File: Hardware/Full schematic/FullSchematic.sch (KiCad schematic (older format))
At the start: 28 parts, among them J1 Conn_01x02, J2 Conn_01x02, J3 Conn_01x02, J4 Conn_01x02, U1 LM358

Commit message: Created VCO testing board
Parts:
- J1, J2, J3, J4: symbol Conn_01x02 -> CONN_01X02
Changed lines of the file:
@@
 EESchema Schematic File Version 2
+LIBS:FullSchematic-rescue
 LIBS:power
 LIBS:device
-LIBS:switches
-LIBS:relays
-LIBS:motors
 LIBS:transistors
 LIBS:conn
@@
 LIBS:valves
 LIBS:fossa library
-LIBS:VCO-cache
+LIBS:FullSchematic-cache
 EELAYER 25 0
 EELAYER END
@@
 encoding utf-8
 Sheet 1 1
-Title "VCO (GPLv3+)"
+Title "Full device (GPLv3+)"
 Date "2018-08-12"
 Rev "2"
@@
 $EndComp
 $Comp
-L Conn_01x02 J1
+L CONN_01X02 J1
 U 1 1 5B720BFC
-P 3550 1900
-F 0 "J1" H 3550 2000 50  0000 C CNN
-F 1 "Conn_01x02" H 3550 1700 50  0000 C CNN
-F 2 "" H 3550 1900 50  0001 C CNN
-F 3 "" H 3550 1900 50  0001 C CNN
-	1    3550 1900
+P 3550 1950
+F 0 "J1" H 3550 2050 50  0000 C CNN
+F 1 "Conn_01x02" H 3550 1750 50  0000 C CNN
+F 2 "" H 3550 1950 50  0001 C CNN
+F 3 "" H 3550 1950 50  0001 C CNN
+	1    3550 1950
 	-1   0    0    -1
 $EndComp
@@
 Tune
 $Comp
-L Conn_01x02 J2
+L CONN_01X02 J2
 U 1 1 5B7237EE
 P 8600 1050
@@
 $EndComp
 $Comp
-L Conn_01x02 J4
+L CONN_01X02 J4
 U 1 1 5B726E8F
-P 9600 2325
-F 0 "J4" H 9600 2425 50  0000 C CNN
-F 1 "Conn_01x02" H 9600 2125 50  0000 C CNN
-F 2 "" H 9600 2325 50  0001 C CNN
-F 3 "" H 9600 2325 50  0001 C CNN
-	1    9600 2325
+P 9600 2375
+F 0 "J4" H 9600 2475 50  0000 C CNN
+F 1 "Conn_01x02" H 9600 2175 50  0000 C CNN
+F 2 "" H 9600 2375 50  0001 C CNN
+F 3 "" H 9600 2375 50  0001 C CNN
+	1    9600 2375
 	1    0    0    -1
 $EndComp
@@
 	1    0    0    -1
 $EndComp
-Text Notes 9700 2400 0    60   ~ 0
+Text Notes 9700 2450 0    60   ~ 0
 Out
 $Comp
@@
 Connection ~ 8400 3475
 $Comp
-L Conn_01x02 J3
+L CONN_01X02 J3
 U 1 1 5BA77BC4
-P 8700 3475
-F 0 "J3" H 8700 3575 50  0000 C CNN
-F 1 "Conn_01x02" H 8700 3275 50  0000 C CNN
-F 2 "" H 8700 3475 50  0001 C CNN
-F 3 "" H 8700 3475 50  0001 C CNN
-	1    8700 3475
-	1    0    0    -1
-$EndComp
-Text Notes 9875 2425 0    60   ~ 0
+P 8700 3525
+F 0 "J3" H 8700 3625 50  0000 C CNN
+F 1 "Conn_01x02" H 8700 3325 50  0000 C CNN
+F 2 "" H 8700 3525 50  0001 C CNN
+F 3 "" H 8700 3525 50  0001 C CNN
+	1    8700 3525
+	1    0    0    -1
+$EndComp
+Text Notes 9875 2475 0    60   ~ 0
 1V peak to peak\n3.5MHz
 Text Notes 8800 3550 0    60   ~ 0

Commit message: Tuning to avoid 6V source instability and make startup stable
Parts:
- removed C6: 0.1uF, symbol C
- C3: value 47pF -> 100pF
- L1: value 27 uH -> 22 uH
- R8: value 110k -> 36k
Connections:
- wire segments 69 -> 68
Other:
- note added: "0V - \nxV - 3.5 MHz\nxV - 3.575 MHz\nxV - 3.65 MHz\n12V -"
- note added: "1.5V peak to peak\n3.5MHz"
- note added: "Signal ground - 6V\nAvoid capacitive load,\nparasitic oscillations may appear!"
- note removed: "1V peak to peak\n3.5MHz"
- note removed: "Signal ground - 6V"
- moved on the sheet: J2
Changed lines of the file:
@@
 P 6500 1550
 F 0 "C3" H 6525 1650 50  0000 L CNN
-F 1 "47pF" H 6525 1450 50  0000 L CNN
+F 1 "100pF" H 6525 1450 50  0000 L CNN
 F 2 "" H 6538 1400 50  0001 C CNN
 F 3 "" H 6500 1550 50  0001 C CNN
@@
 L CONN_01X02 J2
 U 1 1 5B7237EE
-P 8600 1050
-F 0 "J2" H 8600 1150 50  0000 C CNN
-F 1 "Conn_01x02" H 8600 850 50  0000 C CNN
-F 2 "" H 8600 1050 50  0001 C CNN
-F 3 "" H 8600 1050 50  0001 C CNN
-	1    8600 1050
+P 8600 1100
+F 0 "J2" H 8600 1200 50  0000 C CNN
+F 1 "Conn_01x02" H 8600 900 50  0000 C CNN
+F 2 "" H 8600 1100 50  0001 C CNN
+F 3 "" H 8600 1100 50  0001 C CNN
+	1    8600 1100
 	1    0    0    -1
 $EndComp
@@
 P 5600 1975
 F 0 "L1" V 5550 1975 50  0000 C CNN
-F 1 "27 uH" V 5710 1975 50  0000 C CNN
+F 1 "22 uH" V 5710 1975 50  0000 C CNN
 F 2 "" H 5600 1975 50  0001 C CNN
 F 3 "" H 5600 1975 50  0001 C CNN
@@
 P 9050 2325
 F 0 "R8" V 9130 2325 50  0000 C CNN
-F 1 "110k" V 9050 2325 50  0000 C CNN
+F 1 "36k" V 9050 2325 50  0000 C CNN
 F 2 "" V 8980 2325 50  0001 C CNN
 F 3 "" H 9050 2325 50  0001 C CNN
@@
 Wire Wire Line
 	6325 3375 6500 3375
-Wire Wire Line
-	6425 3575 6425 3025
 $Comp
 L +12V #PWR9
@@
 	1    0    0    -1
 $EndComp
-Wire Wire Line
-	6425 3025 7150 3025
 Connection ~ 7150 3475
 $Comp
@@
 Wire Wire Line
 	7100 3475 8500 3475
-Wire Wire Line
-	7150 3025 7150 3625
-Wire Wire Line
-	7150 4000 7150 3925
-$Comp
-L C C6
-U 1 1 5B78B961
-P 7150 3775
-F 0 "C6" H 7175 3875 50  0000 L CNN
-F 1 "0.1uF" H 7175 3675 50  0000 L CNN
-F 2 "" H 7188 3625 50  0001 C CNN
-F 3 "" H 7150 3775 50  0001 C CNN
-	1    7150 3775
-	1    0    0    -1
-$EndComp
-$Comp
-L GND #PWR14
-U 1 1 5B78B9B8
-P 7150 4000
-F 0 "#PWR14" H 7150 3750 50  0001 C CNN
-F 1 "GND" H 7150 3850 50  0000 C CNN
-F 2 "" H 7150 4000 50  0001 C CNN
-F 3 "" H 7150 4000 50  0001 C CNN
-	1    7150 4000
-	1    0    0    -1
-$EndComp
 Connection ~ 4650 2000
 Wire Wire Line
@@
 $EndComp
 Text Notes 9875 2475 0    60   ~ 0
-1V peak to peak\n3.5MHz
-Text Notes 8800 3550 0    60   ~ 0
-Signal ground - 6V
+1.5V peak to peak\n3.5MHz
+Text Notes 8850 3650 0    60   ~ 0
+Signal ground - 6V\nAvoid capacitive load,\nparasitic oscillations may appear!
+Wire Wire Line
+	7150 3475 7150 3100
+Wire Wire Line
+	7150 3100 6425 3100
+Wire Wire Line
+	6425 3100 6425 3575
+Text Notes 3225 1700 0    60   ~ 0
+0V - \nxV - 3.5 MHz\nxV - 3.575 MHz\nxV - 3.65 MHz\n12V -
 $EndSCHEMATC

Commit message: Modifid oscillator (see full schematic) to use 0V-5V tuning voltage.
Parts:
- removed unit 1 of U1
- added VD1: BB135, symbol BB135
- L1: value 22 uH -> 16 uH
- R8: value 36k -> 47k
- renumbered C7 to C6, C8 to C7, VD1 to VD2, VD2 to VD3
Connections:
- wire segments 68 -> 62
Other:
- note added: "0V - 3.152 MHz\n1.45V - 3.5 MHz\n2.02V - 3.575 MHz\n2.75V - 3.65 MHz\n5V - 3.817 MHz"
- note added: "1.7V peak to peak\n3.5MHz"
- note removed: "0V - \nxV - 3.5 MHz\nxV - 3.575 MHz\nxV - 3.65 MHz\n12V -"
- note removed: "1.5V peak to peak\n3.5MHz"
- moved on the sheet: J1, R1, VD2

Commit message: Started experimental firmware implementation
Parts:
- removed C2: 0.1uF, symbol C
- removed J2, J3: Conn_01x02, symbol CONN_01X02
- removed R2, R3: 47k, symbol R
- removed U1: LM358, symbol LM358
- added C12: 0.1uF, symbol FullSchematic-rescue:C
- added C? (x3): 0.1uF, symbol Device:C
- added C?: 100pF, symbol Device:C
- added J? (x2): Conn_01x02_Female, symbol Connector:Conn_01x02_Female
- added J?: Conn_01x04_Female, symbol Connector:Conn_01x04_Female
- added R? (x2): 4.7k, symbol Device:R
- added R?: 18k, symbol Device:R
- added U?: ADF4001, symbol Fossa_library:ADF4001
- added X?: XO53, Oscillator:Oscillator_SMD_EuroQuartz_XO53-4Pin_5.0x3.2mm, symbol Oscillator:XO53
- C1: symbol C -> FullSchematic-rescue:C
- C2: renamed from C3; symbol C -> FullSchematic-rescue:C
- C3: renamed from C4; symbol C -> FullSchematic-rescue:C
- C4: renamed from C5; symbol C -> FullSchematic-rescue:C
- C5: renamed from C6; symbol C -> FullSchematic-rescue:C
- C6: renamed from C7; symbol C -> FullSchematic-rescue:C
- D1, D2: symbol D -> FullSchematic-rescue:D
- DA1: symbol AD8031 -> FullSchematic-rescue:AD8031
- J1, J4: symbol CONN_01X02 -> FullSchematic-rescue:CONN_01X02
- L1: symbol L_Core_Ferrite -> FullSchematic-rescue:L_Core_Ferrite
- R1: symbol R -> FullSchematic-rescue:R
- R2: renamed from R4; symbol R -> FullSchematic-rescue:R
- R3: renamed from R5; symbol R -> FullSchematic-rescue:R
- R4: renamed from R6; symbol R -> FullSchematic-rescue:R
- R5: renamed from R7; symbol R -> FullSchematic-rescue:R
- R6: renamed from R8; symbol R -> FullSchematic-rescue:R
- VD1, VD2, VD3: symbol BB135 -> FullSchematic-rescue:BB135
- VT1: symbol BF862 -> FullSchematic-rescue:BF862
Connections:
- net labels added: +5V, 8MHz_5V_Ref, Fvco3.5, PLL_CLK, PLL_DATA, PLL_LE
- wire segments 62 -> 111
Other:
- note added: "+12V filtered"
- note added: "+5V filtered"
- note added: "0.4V P-P"
- note added: "8 MHz"
- note removed: "+12V"
- note removed: "GND"
- note removed: "Signal ground - 6V\nAvoid capacitive load,\nparasitic oscillations may appear!"
- moved on the sheet: J4, R4, R5

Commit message: Got SPI signal for PLL, some more driver work needed
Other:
- note added: "CLK - PA5\nDATA - PA7\nLE - PA8"
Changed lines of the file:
@@
 Text Notes 4325 4150 0    50   ~ 0
 0.4V P-P
+Text Notes 5400 5100 0    50   ~ 0
+CLK - PA5\nDATA - PA7\nLE - PA8
 $EndSCHEMATC

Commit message: PLL is controllable, Fvco is too weak
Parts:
- removed J1: Conn_01x02, symbol FullSchematic-rescue:CONN_01X02
- added C11: 0.47uF, symbol Device:C
- added C13: 4.7uF, symbol Device:CP
- added R10: 20, symbol Device:R
- gave numbers to parts that had none: 12
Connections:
- net GND: now also C11.2, C13.2
- net Vtune3.5: now reaches R1.2
- net Vtune3.5: now also U1.2 (CP), C11.1, R10.1
- new net: C13.1, R10.2
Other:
- note added: "Kvco=0.133MHz/V"
- note removed: "Tune"

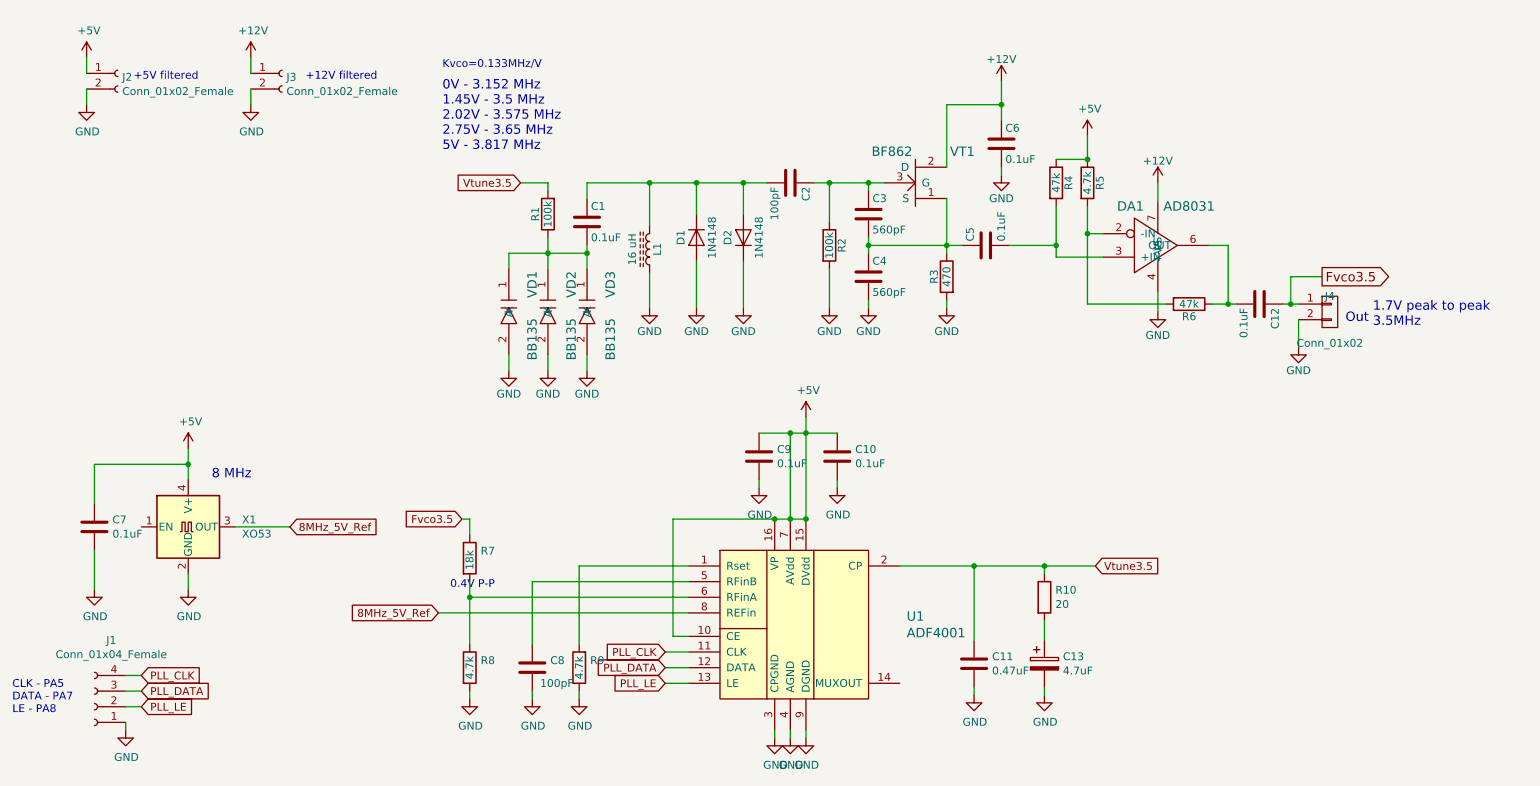
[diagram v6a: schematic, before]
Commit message: Some problems with initialization, but works in general
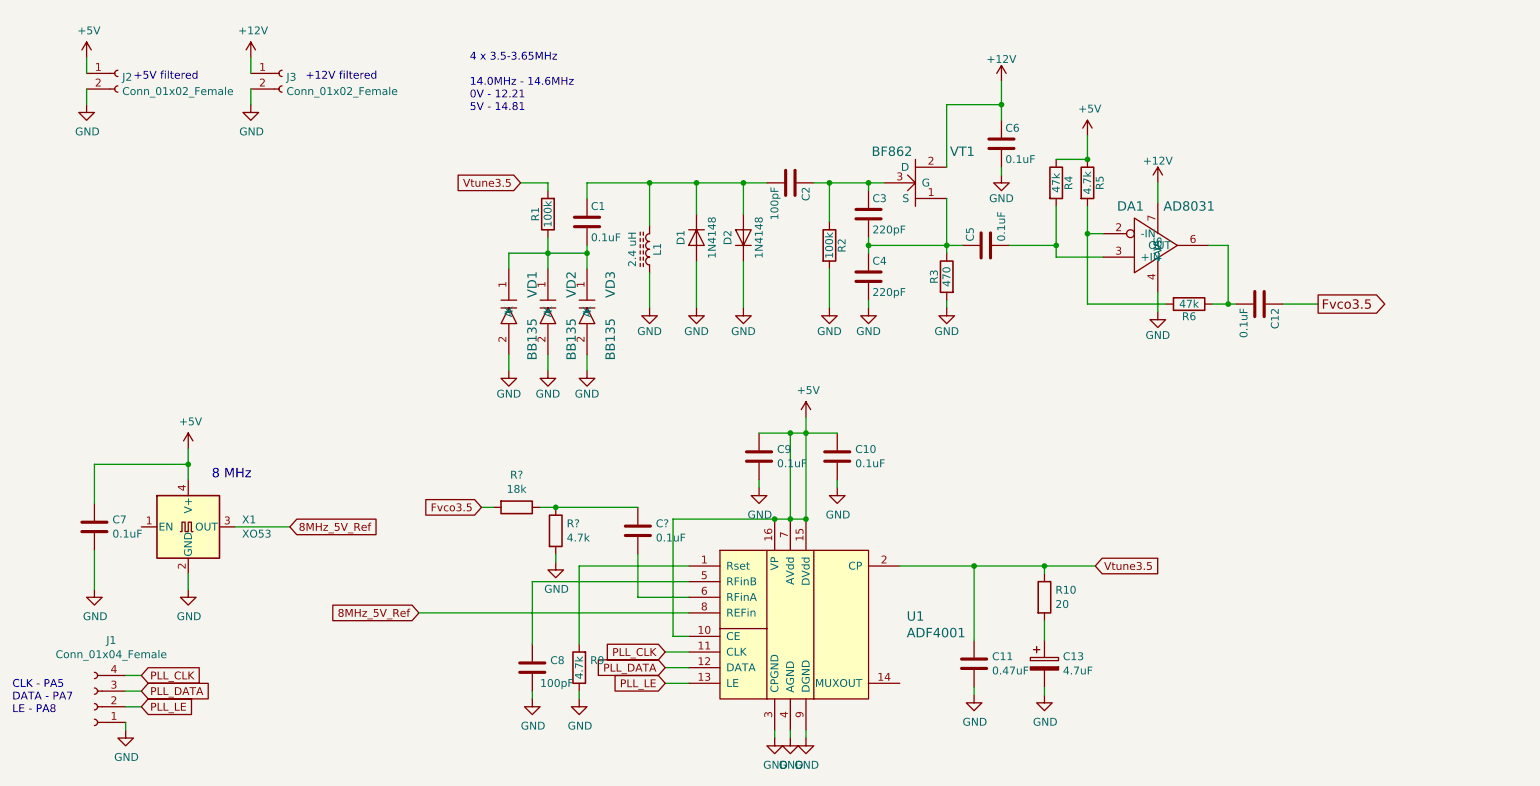
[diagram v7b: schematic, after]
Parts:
- removed J4: Conn_01x02, symbol FullSchematic-rescue:CONN_01X02
- removed R7: 18k, symbol Device:R
- removed R8: 4.7k, symbol Device:R
- added C?: 0.1uF, symbol Device:C
- added R?: 4.7k, symbol Device:R
- added R?: 18k, symbol Device:R
- C3, C4: value 560pF -> 220pF
- L1: value 16 uH -> 2.4 uH
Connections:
- net Fvco3.5: now also R?.2
- net GND: now also R?.2
- net at U1.6 (RFinA): now also C?.2
- new net: C?.1, R?.1, R?.1
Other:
- note added: "4 x 3.5-3.65MHz\n\n14.0MHz - 14.6MHz\n0V - 12.21\n5V - 14.81"
- note removed: "0.4V P-P"
- note removed: "0V - 3.152 MHz\n1.45V - 3.5 MHz\n2.02V - 3.575 MHz\n2.75V - 3.65 MHz\n5V - 3.817 MHz"
- note removed: "1.7V peak to peak\n3.5MHz"
- note removed: "Kvco=0.133MHz/V"
- note removed: "Out"
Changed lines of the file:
@@
 P 7000 1750
 F 0 "C3" H 7025 1850 50  0000 L CNN
-F 1 "560pF" H 7025 1650 50  0000 L CNN
+F 1 "220pF" H 7025 1650 50  0000 L CNN
 F 2 "" H 7038 1600 50  0001 C CNN
 F 3 "" H 7000 1750 50  0001 C CNN
@@
 P 7000 2150
 F 0 "C4" H 7025 2250 50  0000 L CNN
-F 1 "560pF" H 7025 2050 50  0000 L CNN
+F 1 "220pF" H 7025 2050 50  0000 L CNN
 F 2 "" H 7038 2000 50  0001 C CNN
 F 3 "" H 7000 2150 50  0001 C CNN
@@
 $EndComp
 $Comp
-L FullSchematic-rescue:CONN_01X02 J4
-U 1 1 5B726E8F
-P 9950 2375
-F 0 "J4" H 9950 2475 50  0000 C CNN
-F 1 "Conn_01x02" H 9950 2175 50  0000 C CNN
-F 2 "" H 9950 2375 50  0001 C CNN
-F 3 "" H 9950 2375 50  0001 C CNN
-	1    9950 2375
-	1    0    0    -1
-$EndComp
-$Comp
-L FullSchematic-rescue:GND #PWR018
-U 1 1 5B72709E
-P 9750 2600
-F 0 "#PWR018" H 9750 2350 50  0001 C CNN
-F 1 "GND" H 9750 2450 50  0000 C CNN
-F 2 "" H 9750 2600 50  0001 C CNN
-F 3 "" H 9750 2600 50  0001 C CNN
-	1    9750 2600
-	1    0    0    -1
-$EndComp
-Text Notes 10050 2450 0    60   ~ 0
-Out
-$Comp
 L FullSchematic-rescue:GND #PWR05
 U 1 1 5B7892C1
@@
 P 5600 1975
 F 0 "L1" V 5550 1975 50  0000 C CNN
-F 1 "16 uH" V 5710 1975 50  0000 C CNN
+F 1 "2.4 uH" V 5710 1975 50  0000 C CNN
 F 2 "" H 5600 1975 50  0001 C CNN
 F 3 "" H 5600 1975 50  0001 C CNN
@@
 	1    0    0    -1
 $EndComp
-Text Notes 10225 2475 0    60   ~ 0
-1.7V peak to peak\n3.5MHz
-Text Notes 4275 1350 0    60   ~ 0
-0V - 3.152 MHz\n1.45V - 3.5 MHz\n2.02V - 3.575 MHz\n2.75V - 3.65 MHz\n5V - 3.817 MHz
 $Comp
 L FullSchematic-rescue:BB135 VD1
@@
 	1    0    0    -1
 $EndComp
-Text GLabel 9900 2150 2    60   Output ~ 0
+Text GLabel 9875 2325 2    60   Output ~ 0
 Fvco3.5
 Wire Wire Line
@@
 $EndComp
 Wire Wire Line
-	9750 2325 9700 2325
-Wire Wire Line
-	9750 2425 9750 2600
-Wire Wire Line
-	9900 2150 9700 2150
-Wire Wire Line
-	9700 2150 9700 2325
-Connection ~ 9700 2325
-Wire Wire Line
 	7850 1050 7850 1150
 Wire Wire Line
@@
 Wire Wire Line
 	4950 2000 4950 2100
-Wire Wire Line
-	9700 2325 9650 2325
 $Comp
 L Oscillator:XO53 X1
@@
 Wire Wire Line
 	4850 4100 5850 4100
-Text GLabel 4250 4300 0    50   Input ~ 0
+Text GLabel 4125 4300 0    50   Input ~ 0
 8MHz_5V_Ref
-Wire Wire Line
-	5850 4300 4250 4300
-$Comp
-L Device:R R8
-U 1 1 5FE0D1B7
-P 4450 4650
-F 0 "R8" H 4520 4696 50  0000 L CNN
-F 1 "4.7k" V 4450 4575 50  0000 L CNN
-F 2 "" V 4380 4650 50  0001 C CNN
-F 3 "~" H 4450 4650 50  0001 C CNN
-	1    4450 4650
-	1    0    0    -1
-$EndComp
-$Comp
-L FullSchematic-rescue:GND #PWR023
-U 1 1 5FE0EF2A
-P 4450 4850
-F 0 "#PWR023" H 4450 4600 50  0001 C CNN
-F 1 "GND" H 4455 4677 50  0000 C CNN
-F 2 "" H 4450 4850 50  0000 C CNN
-F 3 "" H 4450 4850 50  0000 C CNN
-	1    4450 4850
-	1    0    0    -1
-$EndComp
-Wire Wire Line
-	4450 4850 4450 4800
-$Comp
-L Device:R R7
-U 1 1 5FE18327
-P 4450 3950
-F 0 "R7" H 4520 3996 50  0000 L CNN
-F 1 "18k" V 4450 3875 50  0000 L CNN
-F 2 "" V 4380 3950 50  0001 C CNN
-F 3 "~" H 4450 3950 50  0001 C CNN
-	1    4450 3950
-	1    0    0    -1
-$EndComp
-Wire Wire Line
-	5850 4200 4450 4200
-Wire Wire Line
-	4450 4200 4450 4100
-Wire Wire Line
-	4450 4500 4450 4200
-Connection ~ 4450 4200
-Text GLabel 4400 3700 0    50   Input ~ 0
+Text GLabel 4525 3625 0    50   Input ~ 0
 Fvco3.5
-Wire Wire Line
-	4450 3800 4450 3700
-Wire Wire Line
-	4450 3700 4400 3700
-Text Notes 4325 4150 0    50   ~ 0
-0.4V P-P
 Text Notes 1525 4950 0    50   ~ 0
 CLK - PA5\nDATA - PA7\nLE - PA8
@@
 	7675 4000 7200 4000
 Connection ~ 7675 4000
-Text Notes 4275 825  0    50   ~ 0
-Kvco=0.133MHz/V
 Text GLabel 8450 4000 2    50   Input ~ 0
 Vtune3.5
@@
 	1    0    0    -1
 $EndComp
+Text Notes 4450 1100 0    50   ~ 0
+4 x 3.5-3.65MHz\n\n14.0MHz - 14.6MHz\n0V - 12.21\n5V - 14.81
+Wire Wire Line
+	9650 2325 9875 2325
+Wire Wire Line
+	4125 4300 5850 4300
+$Comp
+L Device:C C?
+U 1 1 5FDE6E98
+P 5525 3775
+F 0 "C?" H 5640 3821 50  0000 L CNN
+F 1 "0.1uF" H 5640 3730 50  0000 L CNN
+F 2 "" H 5563 3625 50  0001 C CNN
+F 3 "~" H 5525 3775 50  0001 C CNN
+	1    5525 3775
+	1    0    0    -1
+$EndComp
+Wire Wire Line
+	5850 4200 5525 4200
+Wire Wire Line
+	5525 4200 5525 3925
+$Comp
+L Device:R R?
+U 1 1 5FDEBFF6
+P 5000 3775
+F 0 "R?" H 5070 3821 50  0000 L CNN
+F 1 "4.7k" H 5070 3730 50  0000 L CNN
+F 2 "" V 4930 3775 50  0001 C CNN
+F 3 "~" H 5000 3775 50  0001 C CNN
+	1    5000 3775
+	1    0    0    -1
+$EndComp
+$Comp
+L Device:R R?
+U 1 1 5FDED040
+P 4750 3625
+F 0 "R?" V 4543 3625 50  0000 C CNN
+F 1 "18k" V 4634 3625 50  0000 C CNN
+F 2 "" V 4680 3625 50  0001 C CNN
+F 3 "~" H 4750 3625 50  0001 C CNN
+	1    4750 3625
+	0    1    1    0
+$EndComp
+Wire Wire Line
+	5000 3625 5525 3625
+$Comp
+L FullSchematic-rescue:GND #PWR?
+U 1 1 5FDF221B
+P 5000 3975
+F 0 "#PWR?" H 5000 3725 50  0001 C CNN
+F 1 "GND" H 5005 3802 50  0000 C CNN
+F 2 "" H 5000 3975 50  0000 C CNN
+F 3 "" H 5000 3975 50  0000 C CNN
+	1    5000 3975
+	1    0    0    -1
+$EndComp
+Wire Wire Line
+	5000 3975 5000 3925
+Wire Wire Line
+	4900 3625 5000 3625
+Connection ~ 5000 3625
+Wire Wire Line
+	4525 3625 4600 3625
 $EndSCHEMATC
